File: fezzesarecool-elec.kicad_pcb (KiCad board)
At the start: 2 copper layers, 65 x 56 mm, 5 parts, among them P1 Conn_02x20_Odd_Even

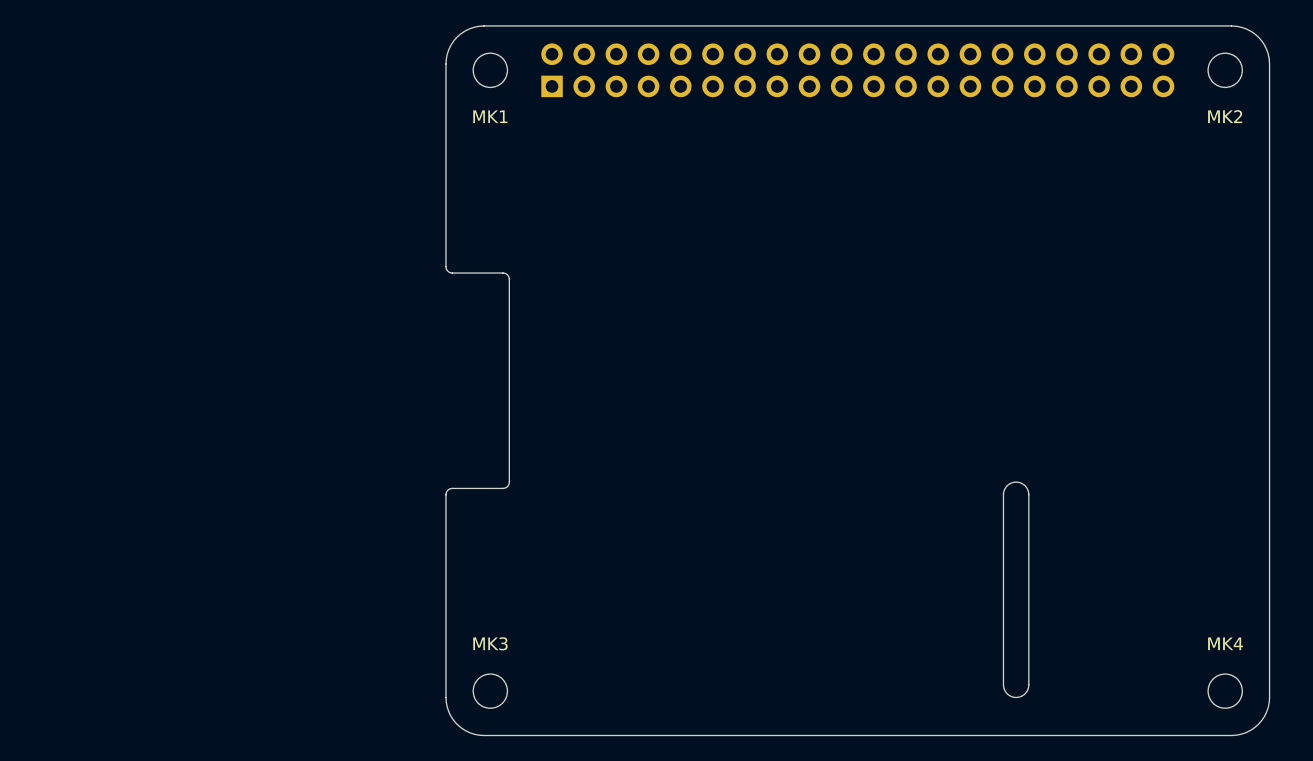
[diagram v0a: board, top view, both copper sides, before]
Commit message: Small schema fixes. PCB basic placement done, now routing.
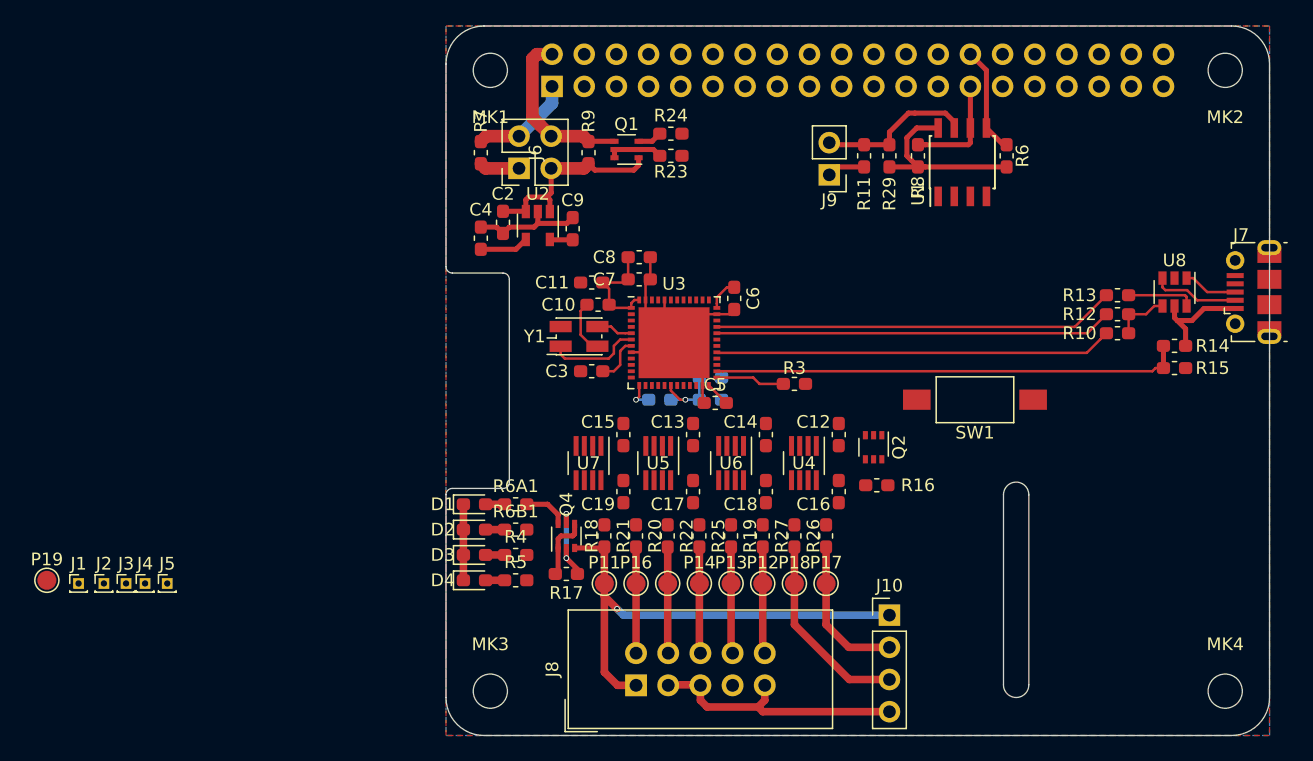
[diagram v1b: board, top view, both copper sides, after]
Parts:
- added C1: 100n, Capacitor_SMD:C_0603_1608Metric_Pad1.05x0.95mm_HandSolder, B.Cu at (220.9, 121.8)
- added C10: 100n, Capacitor_SMD:C_0603_1608Metric_Pad1.05x0.95mm_HandSolder, F.Cu at (212.0, 116.0)
- added C11: 1u, Capacitor_SMD:C_0603_1608Metric_Pad1.05x0.95mm_HandSolder, F.Cu at (211.5, 114.2)
- added C12: 100n, Capacitor_SMD:C_0603_1608Metric_Pad1.05x0.95mm_HandSolder, F.Cu at (231.0, 126.2)
- added C13: 100n, Capacitor_SMD:C_0603_1608Metric_Pad1.05x0.95mm_HandSolder, F.Cu at (219.5, 126.2)
- added C14: 100n, Capacitor_SMD:C_0603_1608Metric_Pad1.05x0.95mm_HandSolder, F.Cu at (225.2, 126.2)
- added C15: 100n, Capacitor_SMD:C_0603_1608Metric_Pad1.05x0.95mm_HandSolder, F.Cu at (214.0, 126.2)
- added C16: 100n, Capacitor_SMD:C_0603_1608Metric_Pad1.05x0.95mm_HandSolder, F.Cu at (231.0, 130.8)
- added C17: 100n, Capacitor_SMD:C_0603_1608Metric_Pad1.05x0.95mm_HandSolder, F.Cu at (219.5, 130.8)
- added C18: 100n, Capacitor_SMD:C_0603_1608Metric_Pad1.05x0.95mm_HandSolder, F.Cu at (225.2, 130.8)
- added C19: 100n, Capacitor_SMD:C_0603_1608Metric_Pad1.05x0.95mm_HandSolder, F.Cu at (214.0, 130.8)
- added C2: 4u7, Capacitor_SMD:C_0603_1608Metric_Pad1.05x0.95mm_HandSolder, F.Cu at (204.5, 109.5)
- added C3: 100n, Capacitor_SMD:C_0603_1608Metric_Pad1.05x0.95mm_HandSolder, F.Cu at (211.5, 121.2)
- added C4: 10n, Capacitor_SMD:C_0603_1608Metric_Pad1.05x0.95mm_HandSolder, F.Cu at (202.8, 110.8)
- added C5: 100n, Capacitor_SMD:C_0603_1608Metric_Pad1.05x0.95mm_HandSolder, F.Cu at (221.2, 123.8)
- added C6: 100n, Capacitor_SMD:C_0603_1608Metric_Pad1.05x0.95mm_HandSolder, F.Cu at (222.8, 115.5)
- added C7: 100n, Capacitor_SMD:C_0603_1608Metric_Pad1.05x0.95mm_HandSolder, F.Cu at (215.2, 114.0)
- added C8: 4u7, Capacitor_SMD:C_0603_1608Metric_Pad1.05x0.95mm_HandSolder, F.Cu at (215.2, 112.2)
- added C9: 4u7, Capacitor_SMD:C_0603_1608Metric_Pad1.05x0.95mm_HandSolder, F.Cu at (210.0, 110.0)
- added D1: Green, Diode_SMD:D_0603_1608Metric_Pad1.05x0.95mm_HandSolder, F.Cu at (202.2, 131.8)
- added D2: Red, Diode_SMD:D_0603_1608Metric_Pad1.05x0.95mm_HandSolder, F.Cu at (202.2, 133.8)
- added D3: Orange, Diode_SMD:D_0603_1608Metric_Pad1.05x0.95mm_HandSolder, F.Cu at (202.2, 135.8)
- added D4: Yellow, Diode_SMD:D_0603_1608Metric_Pad1.05x0.95mm_HandSolder, F.Cu at (202.2, 137.8)
- added J1: Conn_01x01, Connector_PinHeader_1.00mm:PinHeader_1x01_P1.00mm_Vertical, F.Cu at (171.0, 138.0)
- added J10: Conn_01x04, Connector_PinHeader_2.54mm:PinHeader_1x04_P2.54mm_Vertical, F.Cu at (235.0, 140.5)
- added J2: Conn_01x01, Connector_PinHeader_1.00mm:PinHeader_1x01_P1.00mm_Vertical, F.Cu at (173.0, 138.0)
- added J3: Conn_01x01, Connector_PinHeader_1.00mm:PinHeader_1x01_P1.00mm_Vertical, F.Cu at (174.8, 138.0)
- added J4: Conn_01x01, Connector_PinHeader_1.00mm:PinHeader_1x01_P1.00mm_Vertical, F.Cu at (176.2, 138.0)
- added J5: Conn_01x01, Connector_PinHeader_1.00mm:PinHeader_1x01_P1.00mm_Vertical, F.Cu at (178.0, 138.0)
- added J6: CONN_02X02, Connector_PinHeader_2.54mm:PinHeader_2x02_P2.54mm_Vertical, F.Cu at (205.8, 105.2)
- added J7: USB_B_Micro, Connector_USB:USB_Micro-B_Molex-105017-0001, F.Cu at (263.8, 115.0)
- added J8: Conn_ARM_JTAG_SWD_10, Connector_IDC:IDC-Header_2x05_P2.54mm_Vertical, F.Cu at (215.0, 146.0)
- added J9: CONN_01X02, Connector_PinHeader_2.54mm:PinHeader_1x02_P2.54mm_Vertical, F.Cu at (230.2, 105.8)
- added P11: Conn_01x01, TestPoint:TestPoint_Pad_D1.5mm, F.Cu at (212.5, 138.0)
- added P12: Conn_01x01, TestPoint:TestPoint_Pad_D1.5mm, F.Cu at (225.0, 138.0)
- added P13: Conn_01x01, TestPoint:TestPoint_Pad_D1.5mm, F.Cu at (222.5, 138.0)
- added P14: Conn_01x01, TestPoint:TestPoint_Pad_D1.5mm, F.Cu at (220.0, 138.0)
- added P15: Conn_01x01, TestPoint:TestPoint_Pad_D1.5mm, F.Cu at (217.5, 138.0)
- added P16: Conn_01x01, TestPoint:TestPoint_Pad_D1.5mm, F.Cu at (215.0, 138.0)
- added P17: Conn_01x01, TestPoint:TestPoint_Pad_D1.5mm, F.Cu at (230.0, 138.0)
- added P18: Conn_01x01, TestPoint:TestPoint_Pad_D1.5mm, F.Cu at (227.5, 138.0)
- added P19: Conn_01x01, TestPoint:TestPoint_Pad_D1.5mm, F.Cu at (168.5, 137.8)
- added Q1: MMDT5401, Package_TO_SOT_SMD:SOT-363_SC-70-6, F.Cu at (214.2, 103.8)
- added Q2: FDG1024NZ, Package_TO_SOT_SMD:SOT-363_SC-70-6, F.Cu at (233.8, 127.2)
- added Q4: FDG1023NZ, Package_TO_SOT_SMD:SOT-363_SC-70-6, F.Cu at (209.5, 134.2)
- added R1: 4k7, Resistor_SMD:R_0603_1608Metric_Pad1.05x0.95mm_HandSolder, B.Cu at (216.9, 123.5)
- added R10: 1k5, Resistor_SMD:R_0603_1608Metric_Pad1.05x0.95mm_HandSolder, F.Cu at (253.0, 118.2)
- added R11: DNP, Resistor_SMD:R_0603_1608Metric_Pad1.05x0.95mm_HandSolder, F.Cu at (233.0, 104.2)
- added R12: 22E, Resistor_SMD:R_0603_1608Metric_Pad1.05x0.95mm_HandSolder, F.Cu at (253.0, 116.8)
- added R13: 22E, Resistor_SMD:R_0603_1608Metric_Pad1.05x0.95mm_HandSolder, F.Cu at (253.0, 115.2)
- added R14: 4k7, Resistor_SMD:R_0603_1608Metric_Pad1.05x0.95mm_HandSolder, F.Cu at (257.5, 119.2)
- added R15: 10k, Resistor_SMD:R_0603_1608Metric_Pad1.05x0.95mm_HandSolder, F.Cu at (257.5, 121.0)
- added R16: 10k, Resistor_SMD:R_0603_1608Metric_Pad1.05x0.95mm_HandSolder, F.Cu at (234.0, 130.2)
- added R17: 10k, Resistor_SMD:R_0603_1608Metric_Pad1.05x0.95mm_HandSolder, F.Cu at (209.5, 137.2)
- added R18: 100E, Resistor_SMD:R_0603_1608Metric_Pad1.05x0.95mm_HandSolder, F.Cu at (212.5, 134.2)
- added R19: 100E, Resistor_SMD:R_0603_1608Metric_Pad1.05x0.95mm_HandSolder, F.Cu at (225.0, 134.2)
- added R2: 10k, Resistor_SMD:R_0603_1608Metric_Pad1.05x0.95mm_HandSolder, B.Cu at (220.9, 123.5)
- added R20: 100E, Resistor_SMD:R_0603_1608Metric_Pad1.05x0.95mm_HandSolder, F.Cu at (217.5, 134.2)
- added R21: 100E, Resistor_SMD:R_0603_1608Metric_Pad1.05x0.95mm_HandSolder, F.Cu at (215.0, 134.2)
- added R22: 100E, Resistor_SMD:R_0603_1608Metric_Pad1.05x0.95mm_HandSolder, F.Cu at (220.0, 134.2)
- added R23: 22, Resistor_SMD:R_0603_1608Metric_Pad1.05x0.95mm_HandSolder, F.Cu at (217.8, 104.2)
- added R24: 22, Resistor_SMD:R_0603_1608Metric_Pad1.05x0.95mm_HandSolder, F.Cu at (217.8, 102.5)
- added R25: 100E, Resistor_SMD:R_0603_1608Metric_Pad1.05x0.95mm_HandSolder, F.Cu at (222.5, 134.2)
- added R26: 100E, Resistor_SMD:R_0603_1608Metric_Pad1.05x0.95mm_HandSolder, F.Cu at (230.0, 134.2)
- added R27: 100E, Resistor_SMD:R_0603_1608Metric_Pad1.05x0.95mm_HandSolder, F.Cu at (227.5, 134.2)
- added R29: 1K, Resistor_SMD:R_0603_1608Metric_Pad1.05x0.95mm_HandSolder, F.Cu at (235.0, 104.2)
- added R3: 10k, Resistor_SMD:R_0603_1608Metric_Pad1.05x0.95mm_HandSolder, F.Cu at (227.5, 122.2)
- added R4: 330E, Resistor_SMD:R_0603_1608Metric_Pad1.05x0.95mm_HandSolder, F.Cu at (205.5, 135.8)
- added R5: 330E, Resistor_SMD:R_0603_1608Metric_Pad1.05x0.95mm_HandSolder, F.Cu at (205.5, 137.8)
- added R6: 3.9K, Resistor_SMD:R_0603_1608Metric_Pad1.05x0.95mm_HandSolder, F.Cu at (244.2, 104.2)
- added R6A1: 330E, Resistor_SMD:R_0603_1608Metric_Pad1.05x0.95mm_HandSolder, F.Cu at (205.5, 131.8)
- added R6B1: 330E, Resistor_SMD:R_0603_1608Metric_Pad1.05x0.95mm_HandSolder, F.Cu at (205.5, 133.8)
- added R7: DNP, Resistor_SMD:R_0603_1608Metric_Pad1.05x0.95mm_HandSolder, F.Cu at (202.8, 104.0)
- added R8: 3.9K, Resistor_SMD:R_0603_1608Metric_Pad1.05x0.95mm_HandSolder, F.Cu at (237.2, 104.2)
- added R9: DNP, Resistor_SMD:R_0603_1608Metric_Pad1.05x0.95mm_HandSolder, F.Cu at (211.2, 104.0)
- added SW1: SW_DIP_x01, Button_Switch_SMD:SW_SPST_FSMSM, F.Cu at (241.8, 123.5)
- added U1: CAT24C256, Package_SO:SOIC-8_3.9x4.9mm_P1.27mm, F.Cu at (240.8, 104.8)
- added U2: AP131-33, Package_TO_SOT_SMD:SOT-23-5, F.Cu at (207.2, 109.8)
- added U3: STM32F103CBUx, Package_DFN_QFN:QFN-48-1EP_7x7mm_P0.5mm_EP5.6x5.6mm, F.Cu at (218.0, 119.0)
- added U4: SN74LVC2T45, Package_TO_SOT_SMD:SOT-23-8_Handsoldering, F.Cu at (228.2, 128.5)
- added U5: SN74LVC2T45, Package_TO_SOT_SMD:SOT-23-8_Handsoldering, F.Cu at (216.8, 128.5)
- added U6: SN74LVC2T45, Package_TO_SOT_SMD:SOT-23-8_Handsoldering, F.Cu at (222.5, 128.5)
- added U7: SN74LVC2T45, Package_TO_SOT_SMD:SOT-23-8_Handsoldering, F.Cu at (211.2, 128.5)
- added U8: USBLC6-2SC6, Package_TO_SOT_SMD:SOT-23-6, F.Cu at (257.5, 115.0)
- added Y1: 8Mhz, Oscillator:Oscillator_SMD_EuroQuartz_XO32-4Pin_3.2x2.5mm_HandSoldering, F.Cu at (210.5, 118.5)
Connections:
- net +3V3 renamed /P3V3_HAT
- net +5V renamed /P5V_HAT
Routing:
- net GND: track 0.00 -> 70.0 mm
- net /BlackMagicProbev2.1/TPWR: track 0.00 -> 38.3 mm, vias 0 -> 1
- net /BlackMagicProbev2.1/VBUS: track 0.00 -> 37.1 mm
- net /BlackMagicProbev2.1/USB+: track 0.00 -> 31.8 mm
- net Net-(R10-Pad2): track 0.00 -> 31.4 mm
- net /BlackMagicProbev2.1/USB-: track 0.00 -> 31.4 mm
- net +5V: track 0.00 -> 24.6 mm
- net +3V3: track 0.00 -> 18.6 mm
- net /P3V3: track 0.00 -> 17.9 mm
- net /BlackMagicProbev2.1/RXD: track 0.00 -> 15.4 mm
- net /P5V_HAT: track 0.00 -> 13.6 mm
- net Net-(J9-Pad2): track 0.00 -> 12.3 mm
- net /BlackMagicProbev2.1/TXD: track 0.00 -> 11.9 mm
- net /ID_SD: track 0.00 -> 8.65 mm
- net /ID_SC: track 0.00 -> 8.49 mm
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- added copper zone on B.Cu, net GND
- added copper zone on F.Cu, net GND
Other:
- net class Default: via_dia 0.9 -> 0.45; via_drill 0.6 -> 0.3
- rule via_min_drill: 0.5 -> 0.3
- rule via_min_size: 0.8 -> 0.3
- board text removed: "RASPBERRY-PI 40-PIN ADDON BOARD VIEW FROM TOP NOTE: P1 SHOULD BE FITTED ON THE REVERSE OF THE BOARD ADD EDGE CUTS FROM CAMERA AND DISPLAY PORTS AS REQUIRED"

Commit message: pcb changes
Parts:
- removed P11, P12, P13, P14, P15, P16, P17, P18: Conn_01x01, TestPoint:TestPoint_Pad_D1.5mm
- C1, R1, R2: moved to F.Cu
- moved Q4 7.16 mm to (206.5, 140.8), turned to 0 degrees
- moved R17 6.95 mm to (203.5, 140.8), turned to 270 degrees
- moved C1 5.91 mm to (216.2, 125.3), turned to 270 degrees
- moved R18 3.25 mm to (212.5, 137.5)
- moved R19 3.25 mm to (225.0, 137.5)
- moved R20 3.25 mm to (217.5, 137.5)
- moved R21 3.25 mm to (215.0, 137.5)
- moved R22 3.25 mm to (220.0, 137.5)
- moved R25 3.25 mm to (222.5, 137.5)
- moved R26 3.25 mm to (230.0, 137.5)
- moved R27 3.25 mm to (227.5, 137.5)
- moved C12 2.50 mm to (231.0, 128.8)
- moved C13 2.50 mm to (219.5, 128.8)
- moved C14 2.50 mm to (225.2, 128.8)
- moved C15 2.50 mm to (214.0, 128.8)
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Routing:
- net GND: track 70.0 -> 112.4 mm, vias 0 -> 7
- net +3V3: track 18.6 -> 57.4 mm, vias 0 -> 4
- net /BlackMagicProbev2.1/xTPWR: track 0.00 -> 29.9 mm
- net /BlackMagicProbev2.1/xRST: track 0.00 -> 15.6 mm
- net /BlackMagicProbev2.1/xTMS: track 0.00 -> 8.87 mm
- net /BlackMagicProbev2.1/xRXD: track 0.00 -> 8.46 mm
- net /BlackMagicProbev2.1/xTDI: track 0.00 -> 7.76 mm
- net /BlackMagicProbev2.1/xTDO: track 0.00 -> 5.67 mm, vias 0 -> 2
- net /BlackMagicProbev2.1/xTXD: track 0.00 -> 5.14 mm
- net /BlackMagicProbev2.1/xTCK: track 0.00 -> 4.72 mm
- net /BlackMagicProbev2.1/TPWR: track 38.3 -> 41.7 mm
- net /BlackMagicProbev2.1/TDO: track 8.41 -> 5.16 mm
- net /BlackMagicProbev2.1/TXD: track 11.9 -> 8.62 mm
- net /BlackMagicProbev2.1/TMS: track 8.38 -> 5.12 mm
- net /BlackMagicProbev2.1/TDI: track 8.42 -> 5.17 mm
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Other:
- net class Default: via_dia 0.45 -> 0.4
- net class Signal added: clearance 0.175, trace_width 0.2, via_dia 0.4, via_drill 0.3

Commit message: Add nets to rules
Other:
- net class Signal: trace_width 0.2 -> 0.16
- rule trace_min: 0.1524 -> 0.1525
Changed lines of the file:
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@@
     (zone_clearance 0.508)
     (zone_45_only no)
-    (trace_min 0.1524)
+    (trace_min 0.1525)
     (segment_width 0.1)
     (edge_width 0.1)
@@
     (uvia_dia 0.5)
     (uvia_drill 0.1)
-    (add_net /BlackMagicProbev2.1/PWR_BR)
     (add_net /BlackMagicProbev2.1/TPWR)
-    (add_net /BlackMagicProbev2.1/TXD)
-    (add_net /BlackMagicProbev2.1/VBUS)
     (add_net /BlackMagicProbev2.1/xTPWR)
-    (add_net "Net-(C1-Pad1)")
-    (add_net "Net-(C4-Pad1)")
-    (add_net "Net-(D1-Pad2)")
-    (add_net "Net-(D2-Pad2)")
-    (add_net "Net-(D3-Pad2)")
-    (add_net "Net-(D4-Pad2)")
-    (add_net "Net-(J7-Pad2)")
-    (add_net "Net-(J7-Pad3)")
-    (add_net "Net-(J8-Pad7)")
-    (add_net "Net-(J9-Pad2)")
     (add_net "Net-(Q1-Pad2)")
     (add_net "Net-(Q1-Pad3)")
-    (add_net "Net-(Q4-Pad1)")
-    (add_net "Net-(R10-Pad1)")
-    (add_net "Net-(R10-Pad2)")
-    (add_net "Net-(R13-Pad2)")
-    (add_net "Net-(R3-Pad2)")
-    (add_net "Net-(U3-Pad10)")
-    (add_net "Net-(U3-Pad2)")
-    (add_net "Net-(U3-Pad27)")
-    (add_net "Net-(U3-Pad28)")
-    (add_net "Net-(U3-Pad3)")
-    (add_net "Net-(U3-Pad38)")
-    (add_net "Net-(U3-Pad4)")
-    (add_net "Net-(U3-Pad43)")
-    (add_net "Net-(U3-Pad45)")
-    (add_net "Net-(U3-Pad46)")
   )
   (net_class Power ""
@@
   (net_class Signal ""
     (clearance 0.175)
-    (trace_width 0.2)
+    (trace_width 0.16)
     (via_dia 0.4)
     (via_drill 0.3)
@@
     (add_net /BlackMagicProbev2.1/LED1)
     (add_net /BlackMagicProbev2.1/LED2)
+    (add_net /BlackMagicProbev2.1/PWR_BR)
     (add_net /BlackMagicProbev2.1/RST)
     (add_net /BlackMagicProbev2.1/RXD)
@@
     (add_net /BlackMagicProbev2.1/TMS)
     (add_net /BlackMagicProbev2.1/TRACESWO)
+    (add_net /BlackMagicProbev2.1/TXD)
     (add_net /BlackMagicProbev2.1/USB+)
     (add_net /BlackMagicProbev2.1/USB-)
+    (add_net /BlackMagicProbev2.1/VBUS)
     (add_net /BlackMagicProbev2.1/iRST)
     (add_net /BlackMagicProbev2.1/iRST_SENSE)
@@
     (add_net /ID_SC)
     (add_net /ID_SD)
+    (add_net "Net-(C1-Pad1)")
+    (add_net "Net-(C4-Pad1)")
+    (add_net "Net-(D1-Pad2)")
+    (add_net "Net-(D2-Pad2)")
+    (add_net "Net-(D3-Pad2)")
+    (add_net "Net-(D4-Pad2)")
+    (add_net "Net-(J7-Pad2)")
+    (add_net "Net-(J7-Pad3)")
+    (add_net "Net-(J8-Pad7)")
+    (add_net "Net-(J9-Pad2)")
+    (add_net "Net-(Q4-Pad1)")
+    (add_net "Net-(R10-Pad1)")
+    (add_net "Net-(R10-Pad2)")
+    (add_net "Net-(R13-Pad2)")
+    (add_net "Net-(R3-Pad2)")
+    (add_net "Net-(U3-Pad10)")
+    (add_net "Net-(U3-Pad2)")
+    (add_net "Net-(U3-Pad27)")
+    (add_net "Net-(U3-Pad28)")
+    (add_net "Net-(U3-Pad3)")
+    (add_net "Net-(U3-Pad38)")
+    (add_net "Net-(U3-Pad4)")
+    (add_net "Net-(U3-Pad43)")
+    (add_net "Net-(U3-Pad45)")
+    (add_net "Net-(U3-Pad46)")
   )
   (module Package_TO_SOT_SMD:SOT-363_SC-70-6 (layer F.Cu)

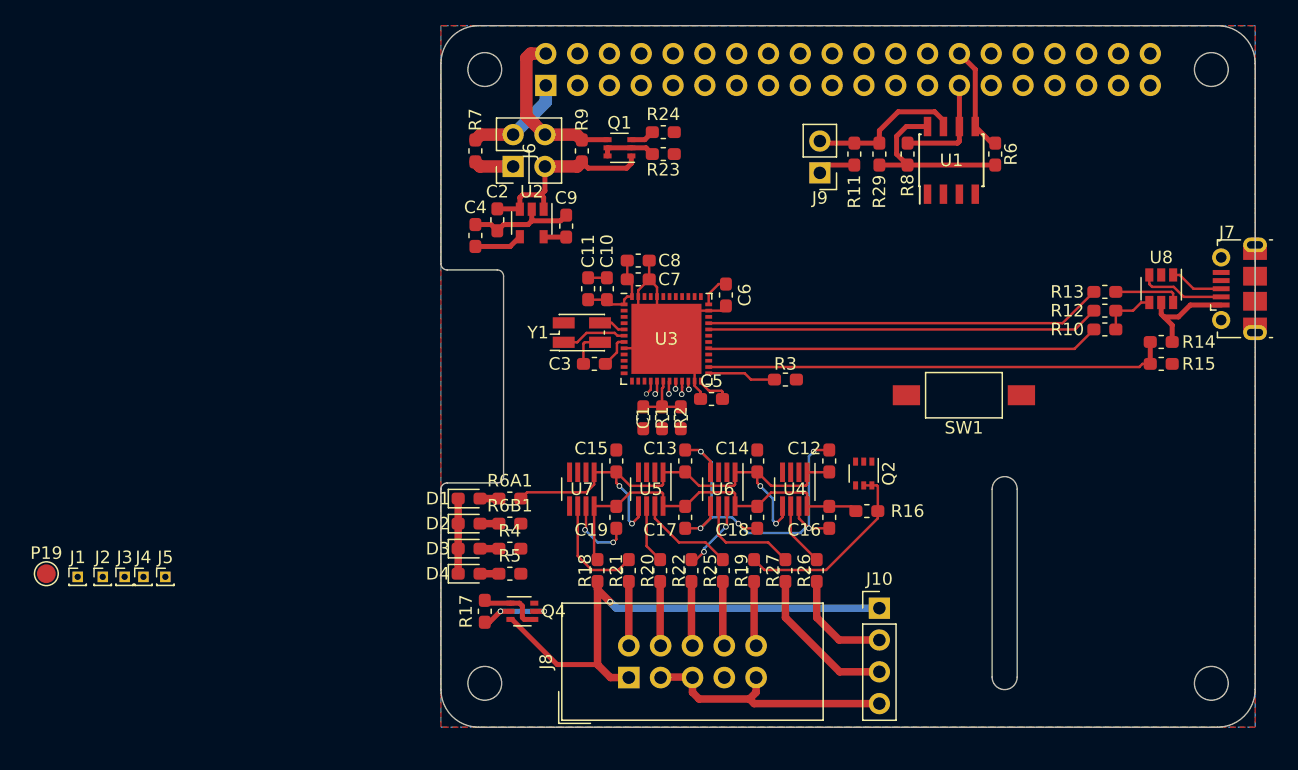
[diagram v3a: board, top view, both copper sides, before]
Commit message: small schema fixes. All is connected on pcb.
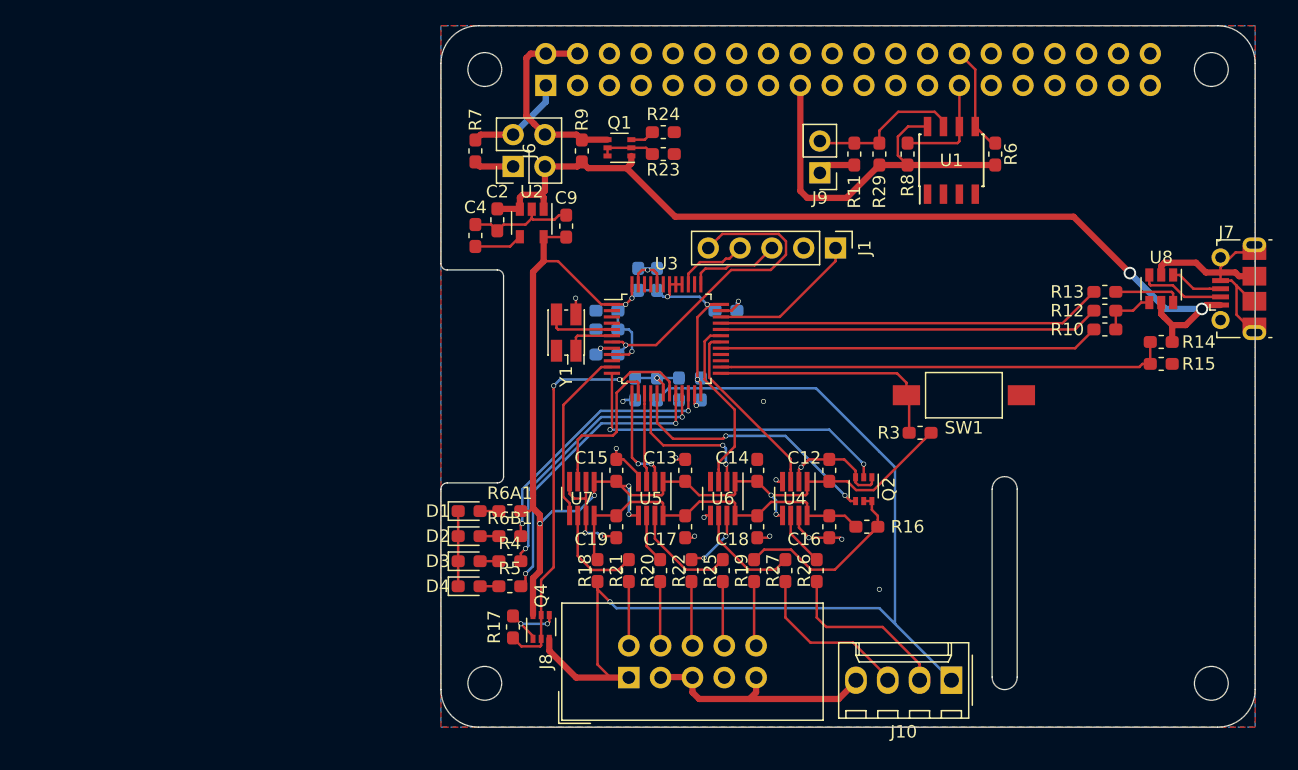
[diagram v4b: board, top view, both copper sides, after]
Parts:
- removed J2, J3, J4, J5: Conn_01x01, Connector_PinHeader_1.00mm:PinHeader_1x01_P1.00mm_Vertical
- removed P19: Conn_01x01, TestPoint:TestPoint_Pad_D1.5mm
- C1, C10, C11, C3, C5, C6, C7, C8, R1, R2: moved to B.Cu
- J1: value Conn_01x01 -> Conn_01x05; footprint Connector_PinHeader_1.00mm:PinHeader_1x01_P1.00mm_Vertical -> Connector_PinHeader_2.54mm:PinHeader_1x05_P2.54mm_Vertical
- J10: footprint Connector_PinHeader_2.54mm:PinHeader_1x04_P2.54mm_Vertical -> Connector_Molex:Molex_KK-254_AE-6410-04A_1x04_P2.54mm_Vertical
- U3: value STM32F103CBUx -> STM32F103CBTx; footprint Package_DFN_QFN:QFN-48-1EP_7x7mm_P0.5mm_EP5.6x5.6mm -> Package_QFP:LQFP-48_7x7mm_P0.5mm
- moved J1 65.9 mm to (231.5, 111.8), turned to 270 degrees
- moved R3 11.6 mm to (238.2, 126.5)
- moved J10 8.13 mm to (240.8, 146.2), turned to 180 degrees
- moved R2 4.31 mm to (215.5, 123.0)
- moved C1 3.66 mm to (219.0, 123.0)
- moved C10 3.25 mm to (213.2, 118.2), turned to 0 degrees
- moved R17 2.57 mm to (205.8, 142.0)
- moved R1 2.33 mm to (217.2, 123.0)
- moved C11 2.30 mm to (213.2, 116.8), turned to 0 degrees
- moved C8 2.12 mm to (217.2, 114.2), turned to 270 degrees
- moved Q4 1.95 mm to (208.0, 142.0), turned to 90 degrees
- moved C3 1.25 mm to (213.2, 120.2)
- moved C6 1.25 mm to (222.8, 116.8), turned to 180 degrees
- moved Q2 1.25 mm to (233.8, 131.0)
- moved R16 1.25 mm to (234.0, 134.0)
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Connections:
- J1 pad 1: /BlackMagicProbev2.1/TRACESWO -> /BlackMagicProbev2.1/SWDIO
- R29 pad 1: /P3V3 -> /P3V3_HAT
- R6 pad 1: /P3V3 -> /P3V3_HAT
- R8 pad 1: /P3V3 -> /P3V3_HAT
- U1 pad 8: /P3V3 -> /P3V3_HAT
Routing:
- net +3V3: track 57.4 -> 116.1 mm, vias 4 -> 12
- net +5V: track 24.6 -> 74.8 mm, vias 0 -> 2
- net /BlackMagicProbev2.1/TPWR: track 41.7 -> 84.1 mm
- net /P3V3_HAT: track 8.20 -> 38.8 mm
- net /BlackMagicProbev2.1/iRST: track 0.00 -> 27.0 mm, vias 0 -> 2
- net /BlackMagicProbev2.1/PWR_BR: track 7.76 -> 34.7 mm, vias 3 -> 2
- net /BlackMagicProbev2.1/LED0: track 0.64 -> 24.0 mm, vias 1 -> 2
- net /BlackMagicProbev2.1/~RST: track 2.65 -> 26.0 mm, vias 0 -> 1
- net /BlackMagicProbev2.1/LED1: track 1.06 -> 23.1 mm, vias 1 -> 2
- net /BlackMagicProbev2.1/LED2: track 0.68 -> 21.1 mm, vias 1 -> 2
- net /BlackMagicProbev2.1/iRST_SENSE: track 1.09 -> 21.0 mm, vias 1 -> 2
- net /P3V3: track 17.9 -> 3.16 mm
- net /BlackMagicProbev2.1/iTXD: track 0.00 -> 14.7 mm
- net /BlackMagicProbev2.1/iRXD: track 0.00 -> 14.2 mm
- net /BlackMagicProbev2.1/iTMS_DIR: track 0.00 -> 14.2 mm
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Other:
- net class Signal: trace_width 0.16 -> 0.2
